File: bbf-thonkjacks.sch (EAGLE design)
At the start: 7 parts, among them J1 WQP-PJ301M-12_JACK, J2 WQP-PJ301M-12_JACK, J3 WQP-PJ301M-12_JACK, J4 WQP-PJ301M-12_JACK

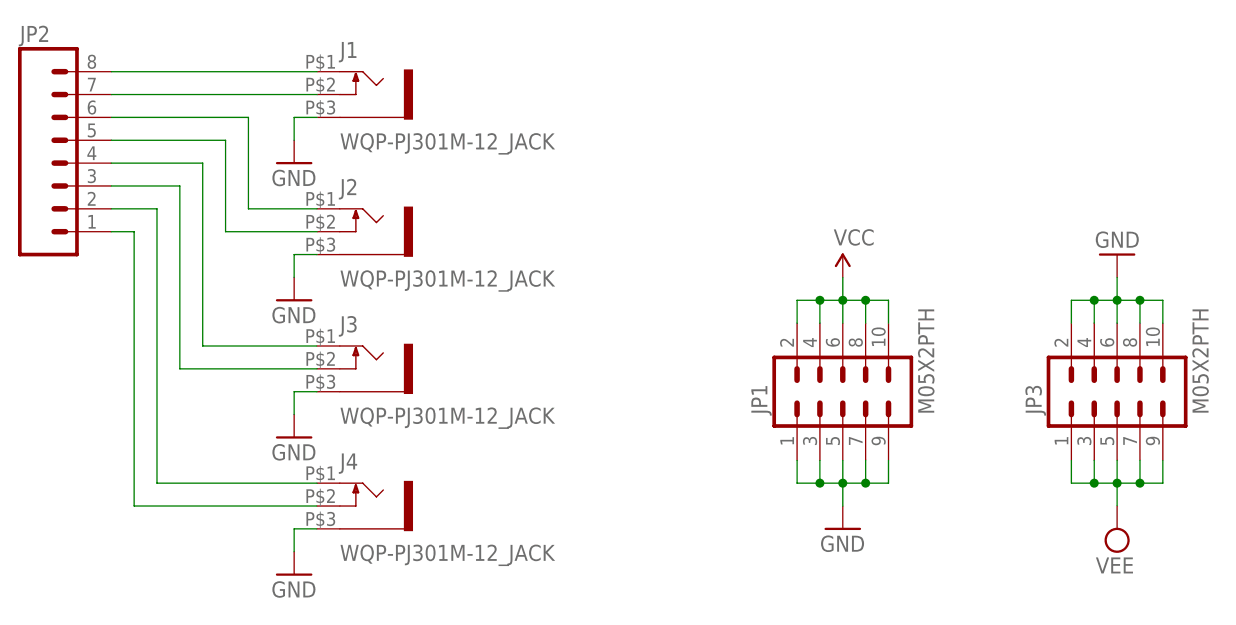
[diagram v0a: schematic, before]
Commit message: thonkiconn jacks wider
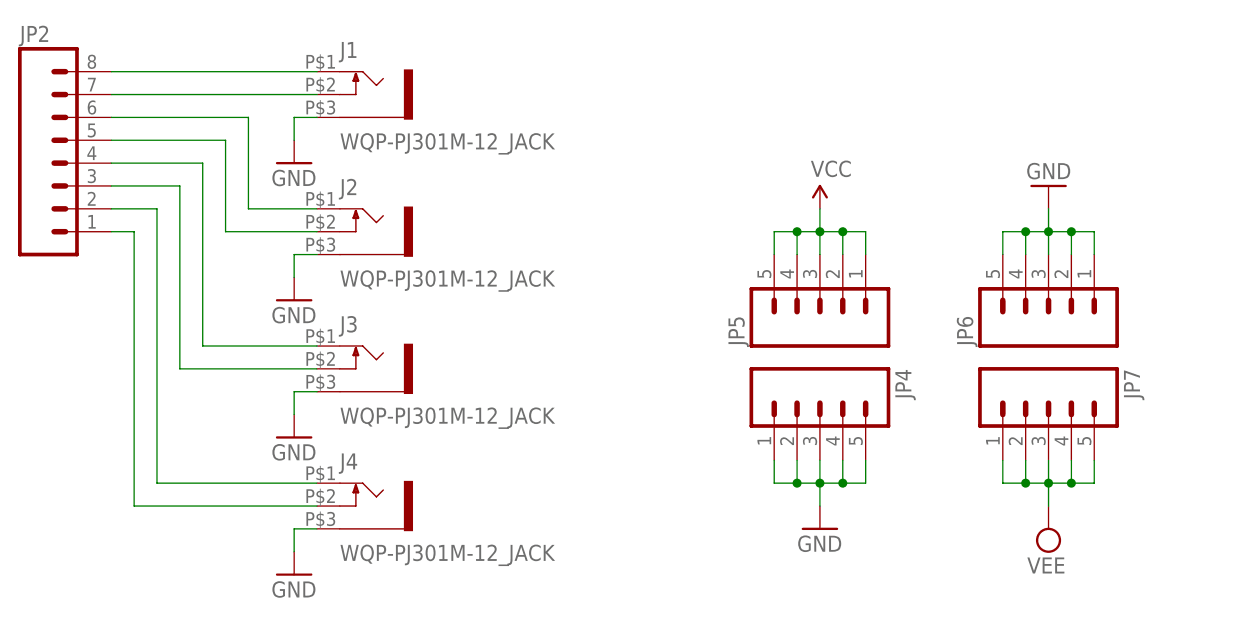
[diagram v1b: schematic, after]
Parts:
- removed JP1, JP3: M05X2PTH, SparkFun:M05X2PTH
- added JP4, JP5, JP6, JP7: (no value), SparkFun:M05PTH
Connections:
- net GND: now also JP4.1, JP4.2, JP4.3, JP4.4, JP4.5, JP6.1, JP6.2, JP6.3, JP6.4, JP6.5; no longer JP1.1, JP1.3, JP1.5, JP1.7, JP1.9, JP3.10, JP3.2, JP3.4, JP3.6, JP3.8
- net VCC: now also JP5.1, JP5.2, JP5.3, JP5.4, JP5.5; no longer JP1.10, JP1.2, JP1.4, JP1.6, JP1.8
- net VEE: now also JP7.1, JP7.2, JP7.3, JP7.4, JP7.5; no longer JP3.1, JP3.3, JP3.5, JP3.7, JP3.9
